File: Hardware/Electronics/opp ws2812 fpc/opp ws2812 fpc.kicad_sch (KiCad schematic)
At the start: 21 parts, among them J1 Conn_01x08

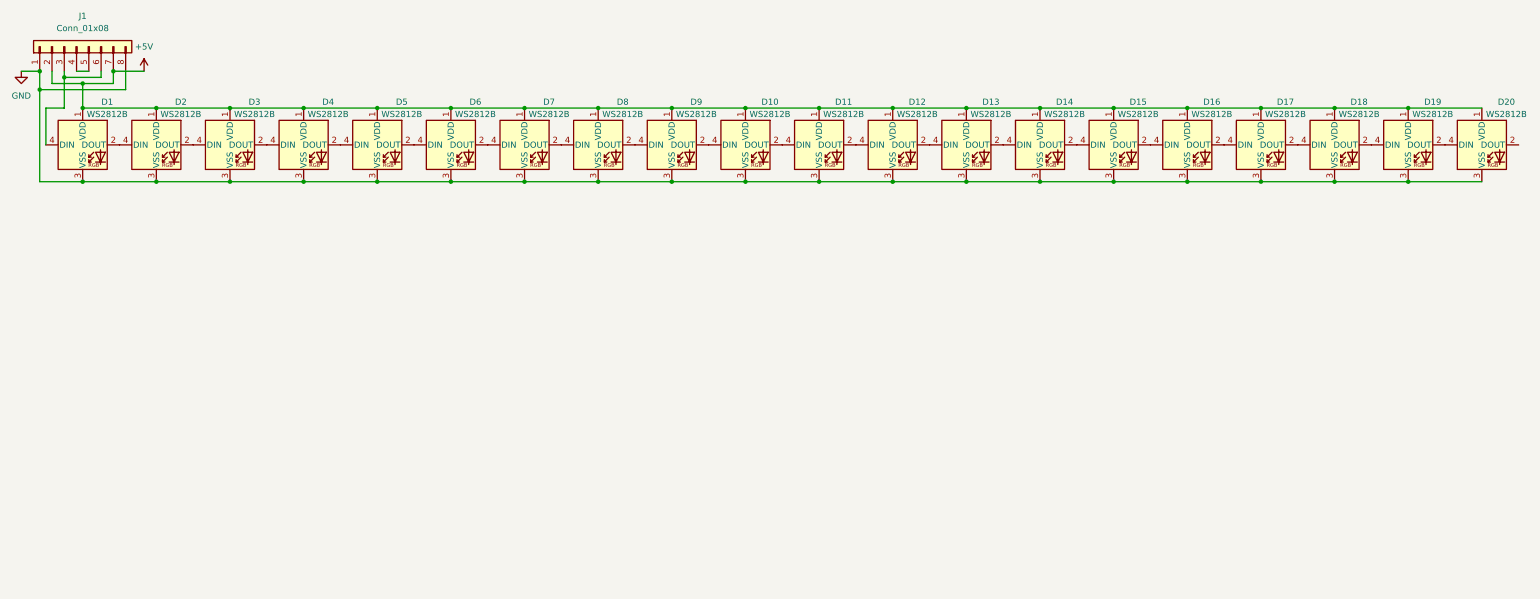
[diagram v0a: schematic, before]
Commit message: Add 20 and 55 pixel strips
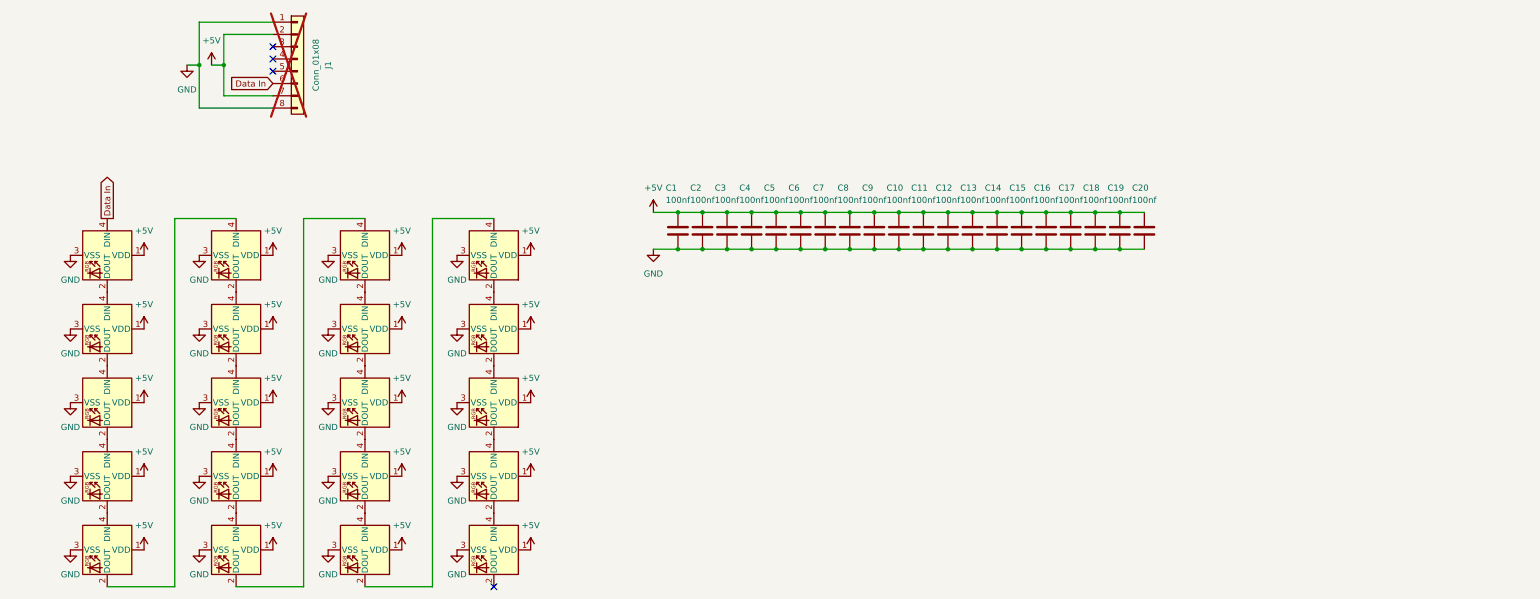
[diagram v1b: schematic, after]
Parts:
- added C1, C10, C11, C12, C13, C14, C15, C16, C17, C18, C19, C2, C20, C3, C4, C5, C6, C7, C8, C9: 100nf, Capacitor_SMD:C_0402_1005Metric, symbol Device:C
- D1, D10, D11, D12, D13, D14, D15, D16, D17, D18, D19, D2, D20, D3, D4, D5, D6, D7, D8, D9: LCSC (none) -> C2843785
- J1: now not fitted; now left out of the parts list
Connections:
- net +5V: now also C1.1, C10.1, C11.1, C12.1, C13.1, C14.1, C15.1, C16.1, C17.1, C18.1, C19.1, C2.1, C20.1, C3.1, C4.1, C5.1, C6.1, C7.1, C8.1, C9.1
- net GND: now also C1.2, C10.2, C11.2, C12.2, C13.2, C14.2, C15.2, C16.2, C17.2, C18.2, C19.2, C2.2, C20.2, C3.2, C4.2, C5.2, C6.2, C7.2, C8.2, C9.2
- net Data In: now reaches D1.4 (DIN), J1.6 (Pin_6)
- net Data In: no longer J1.3 (Pin_3)
- net at J1.4 (Pin_4): no longer J1.5 (Pin_5)
- no-connect marks 0 -> 4
